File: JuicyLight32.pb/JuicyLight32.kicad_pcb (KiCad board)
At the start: 2 copper layers, 66 x 22.5 mm, 40 parts, among them J1 SM06B, J2 USB_A, Q1 BSS138, SW1 SW_Push, U1 STM32F042F6Px, U2 NJM2896F33

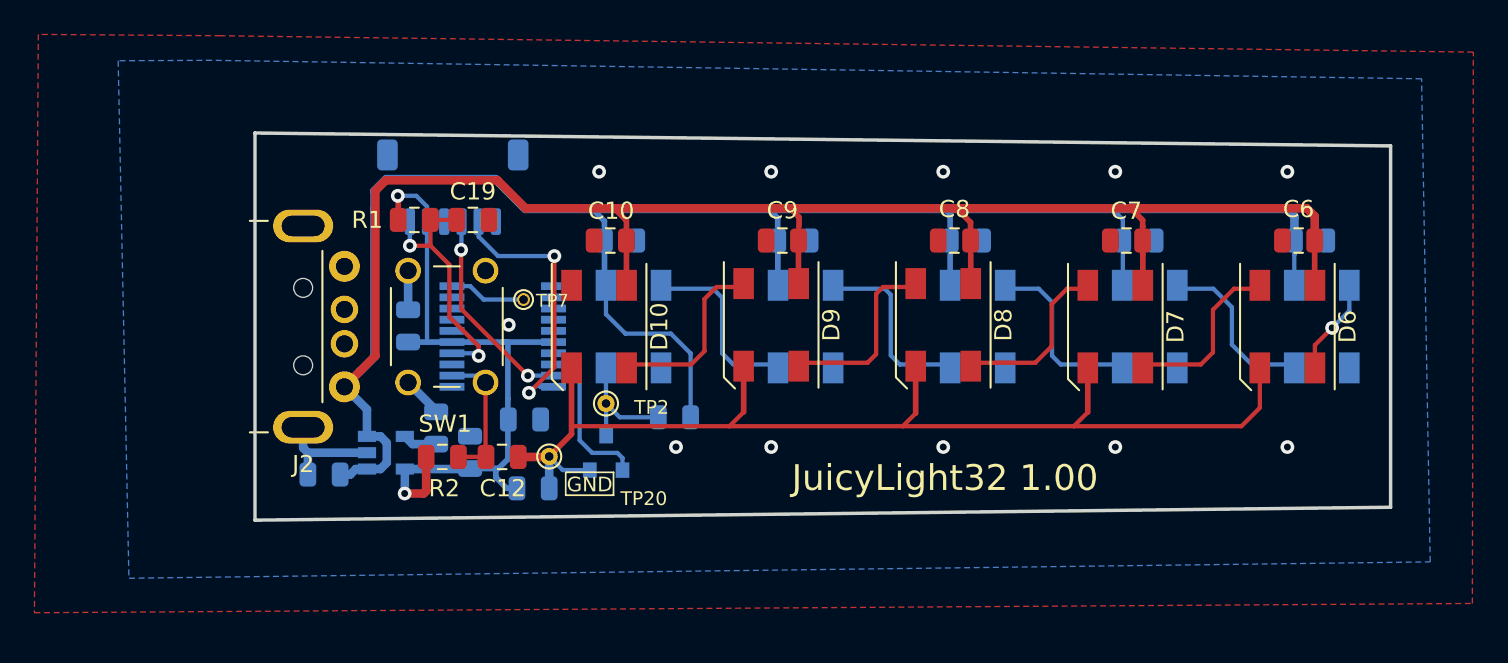
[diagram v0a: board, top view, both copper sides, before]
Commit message: Add pattern 'DD' in dynamic mode.
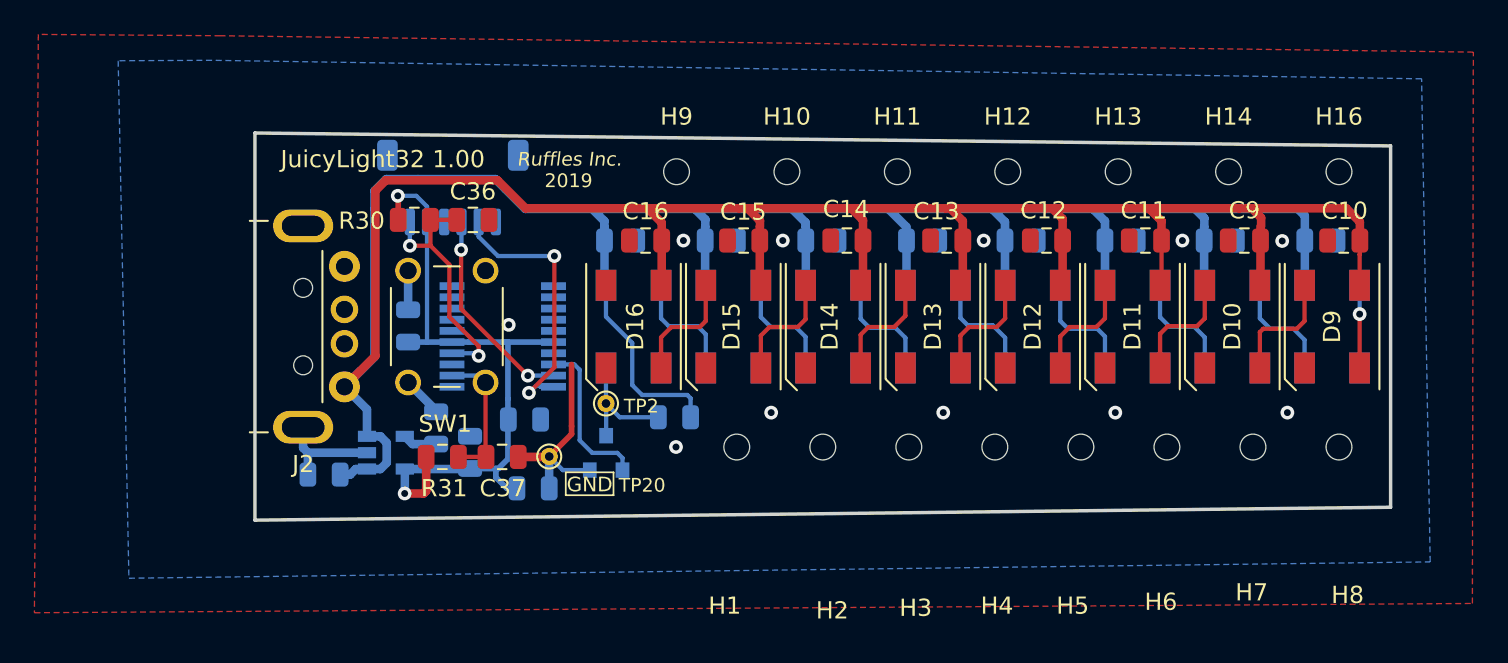
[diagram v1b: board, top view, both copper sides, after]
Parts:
- removed TP7: TestPoint, TestPoint:TestPoint_THTPad_D1.0mm_Drill0.5mm
- added C11: 0.1u, Capacitor_SMD:C_0805_2012Metric, F.Cu at (151.8, 95.0)
- added C12: 0.1u, Capacitor_SMD:C_0805_2012Metric, F.Cu at (146.0, 95.0)
- added C13: 0.1u, Capacitor_SMD:C_0805_2012Metric, F.Cu at (140.2, 95.0)
- added C14: 0.1u, Capacitor_SMD:C_0805_2012Metric, F.Cu at (134.4, 95.0)
- added C15: 0.1u, Capacitor_SMD:C_0805_2012Metric, F.Cu at (128.4, 95.0)
- added C16: 0.1u, Capacitor_SMD:C_0805_2012Metric, F.Cu at (122.7, 95.0)
- added D11: WS2812B, JuicyLight:OST45050C1A, F.Cu at (151.0, 100.0)
- added D12: WS2812B, JuicyLight:OST45050C1A, F.Cu at (145.2, 100.0)
- added D13: WS2812B, JuicyLight:OST45050C1A, F.Cu at (139.4, 100.0)
- added D14: WS2812B, JuicyLight:OST45050C1A, F.Cu at (133.6, 100.0)
- added D15: WS2812B, JuicyLight:OST45050C1A, F.Cu at (127.8, 100.0)
- added D16: WS2812B, JuicyLight:OST45050C1A, F.Cu at (122.0, 100.0)
- added H1: MountingHole, JuicyLight:Hole, F.Cu at (128.0, 107.0)
- added H10: MountingHole, JuicyLight:Hole, F.Cu at (130.9, 91.0)
- added H11: MountingHole, JuicyLight:Hole, F.Cu at (137.3, 91.0)
- added H12: MountingHole, JuicyLight:Hole, F.Cu at (143.7, 91.0)
- added H13: MountingHole, JuicyLight:Hole, F.Cu at (150.2, 91.0)
- added H14: MountingHole, JuicyLight:Hole, F.Cu at (156.6, 91.0)
- added H16: MountingHole, JuicyLight:Hole, F.Cu at (163.0, 91.0)
- added H2: MountingHole, JuicyLight:Hole, F.Cu at (133.0, 107.0)
- added H3: MountingHole, JuicyLight:Hole, F.Cu at (138.0, 107.0)
- added H4: MountingHole, JuicyLight:Hole, F.Cu at (143.0, 107.0)
- added H5: MountingHole, JuicyLight:Hole, F.Cu at (148.0, 107.0)
- added H6: MountingHole, JuicyLight:Hole, F.Cu at (153.0, 107.0)
- added H7: MountingHole, JuicyLight:Hole, F.Cu at (158.0, 107.0)
- added H8: MountingHole, JuicyLight:Hole, F.Cu at (163.0, 107.0)
- added H9: MountingHole, JuicyLight:Hole, F.Cu at (124.5, 91.0)
- C6, C7, C8, D6, D7, D8: moved to B.Cu
- moved C10 42.6 mm to (163.3, 95.0)
- moved D10 36.8 mm to (156.8, 100.0)
- moved D9 32.6 mm to (162.6, 100.0)
- moved C9 26.8 mm to (157.5, 95.0)
- moved D8 22.6 mm to (162.6, 100.0)
- moved C8 21.3 mm to (161.9, 95.0), turned to 0 degrees
- moved C5 16.8 mm to (144.5, 95.0)
- moved D5 16.8 mm to (145.2, 100.0)
- moved D4 12.6 mm to (139.4, 100.0)
- moved C4 12.6 mm to (138.8, 95.0)
- moved C6 10.3 mm to (150.3, 95.0), turned to 0 degrees
- moved D6 9.00 mm to (151.0, 100.0)
- moved C3 8.40 mm to (132.9, 95.0)
- moved D3 8.40 mm to (133.6, 100.0)
- moved D7 6.80 mm to (156.8, 100.0)
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- renumbered C11 to C30, Cd to C31, C31 to C32, C32 to C33, C15 to C34, C16 to C35, C19 to C36, C12 to C37, R1 to R30, R2 to R31, R30 to R32
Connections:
- D10 pad 2: Net-(D10-Pad2) -> /D10OUT
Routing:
- net GND: track 78.2 -> 23.3 mm
- net +5V: track 202.2 -> 236.3 mm
- net /D10OUT: track 0.00 -> 6.47 mm
- net /D14OUT: track 0.00 -> 6.46 mm
- net /D15OUT: track 0.00 -> 6.44 mm
- net /D12OUT: track 0.00 -> 6.41 mm
- net /D11OUT: track 0.00 -> 6.38 mm
- net /D13OUT: track 0.00 -> 6.36 mm
- net /D8OUT: track 10.7 -> 4.40 mm, vias 0 -> 1
- net Net-(U1-Pad10): track 4.48 -> 0.00 mm
- net /D2OUT: track 10.7 -> 6.33 mm
- net /D3OUT: track 10.5 -> 6.36 mm
- net /D1OUT: track 10.5 -> 6.46 mm
- net /D9OUT: track 10.4 -> 6.62 mm
- net /D6OUT: track 10.1 -> 6.31 mm
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
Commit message: R2.0
Board Revision 2.0
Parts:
- removed H1, H10, H11, H12, H13, H14, H16, H2, H3, H4, H5, H6, H7, H8, H9: MountingHole, JuicyLight:Hole
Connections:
- J1 pad MP: (no net) -> GND
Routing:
- net GND: track 23.3 -> 17.4 mm, vias 11 -> 23
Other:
- outline, holes or cut-outs redrawn
- board text added: "JuicyLight32 2.0"
- board text removed: "JuicyLight32 1.00"
